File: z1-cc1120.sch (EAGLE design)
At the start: 12 parts, among them X1 PN61729-S

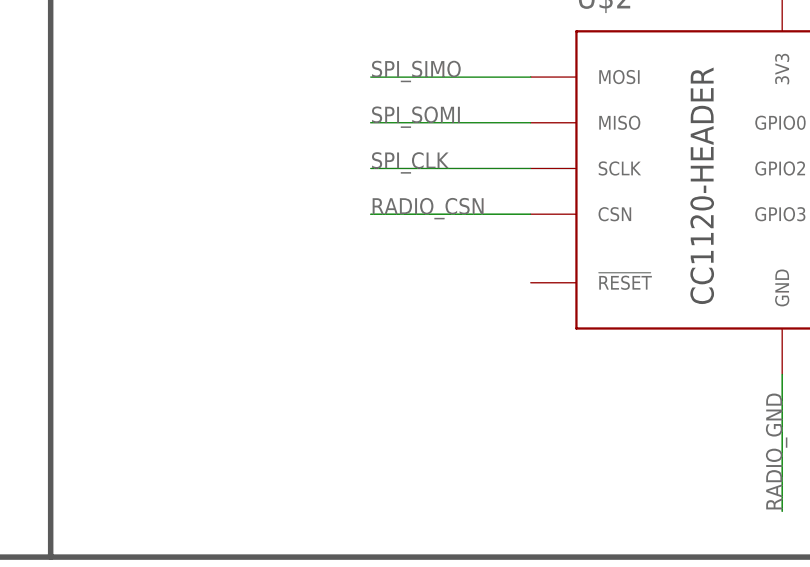
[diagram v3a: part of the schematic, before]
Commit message: !RESET pullup added
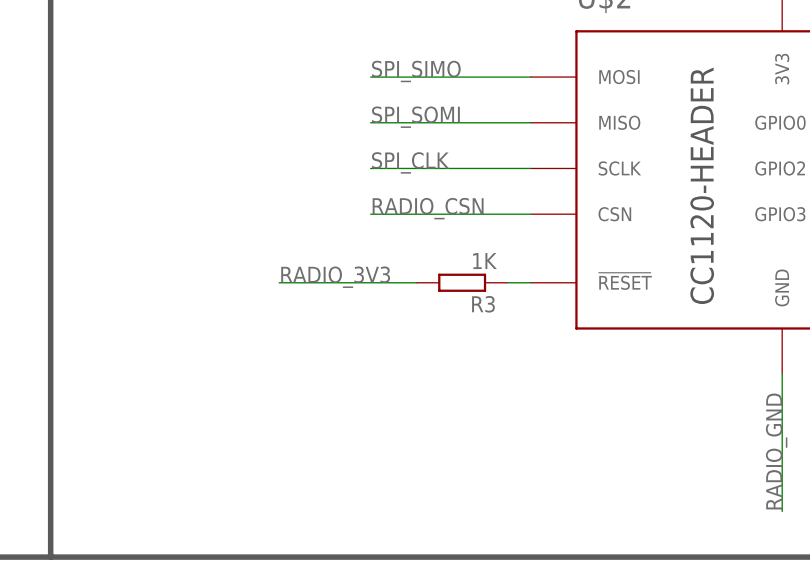
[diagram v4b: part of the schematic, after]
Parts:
- added R3: 1K, resistor:R-EU_R0805
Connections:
- new net N$1: R3.1, U$2.!RESET
- net RADIO_3V3: now also R3.2
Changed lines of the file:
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@@
 <part name="JP1" library="pinhead" deviceset="PINHD-1X6" device=""/>
 <part name="GND3" library="supply1" deviceset="GND" device=""/>
+<part name="R3" library="resistor" deviceset="R-EU_" device="R0805" value="1K"/>
 </parts>
 <sheets>
@@
 <instance part="JP1" gate="A" x="172.72" y="152.4"/>
 <instance part="GND3" gate="1" x="160.02" y="144.78"/>
+<instance part="R3" gate="G$1" x="175.26" y="93.98" rot="R180"/>
 </instances>
 <busses>
@@
 <wire x1="165.1" y1="45.72" x2="182.88" y2="45.72" width="0.1524" layer="91"/>
 </segment>
-</net>
+<segment>
+<pinref part="R3" gate="G$1" pin="2"/>
+<wire x1="170.18" y1="93.98" x2="154.94" y2="93.98" width="0.1524" layer="91"/>
+<label x="154.94" y="93.98" size="1.778" layer="95"/>
+</segment>
+</net>
+<net name="N$1" class="0">
+<segment>
+<pinref part="U$2" gate="G$1" pin="!RESET"/>
+<pinref part="R3" gate="G$1" pin="1"/>
+<wire x1="182.88" y1="93.98" x2="180.34" y2="93.98" width="0.1524" layer="91"/>
+</segment>
+</net>

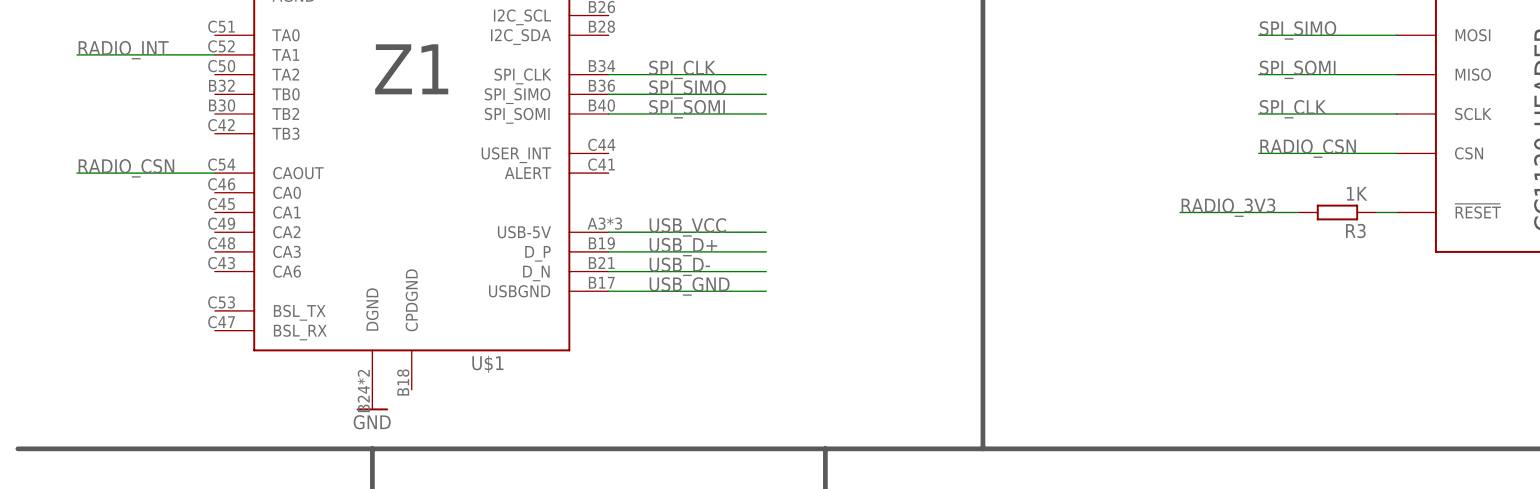
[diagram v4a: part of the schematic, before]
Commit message: Added reset line from msp to cc1120
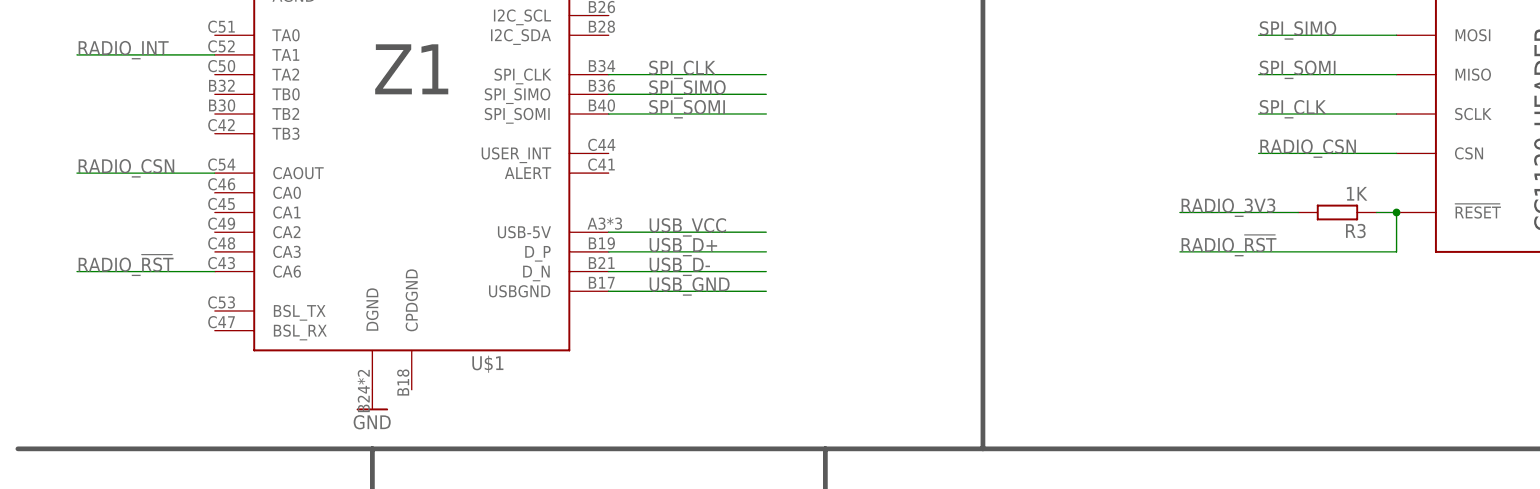
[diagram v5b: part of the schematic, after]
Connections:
- removed net N$1: R3.1, U$2.!RESET
- new net RADIO_!RST: R3.1, U$1.CA6, U$2.!RESET
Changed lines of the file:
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@@
 </segment>
 </net>
-<net name="N$1" class="0">
+<net name="RADIO_!RST" class="0">
 <segment>
 <pinref part="U$2" gate="G$1" pin="!RESET"/>
 <pinref part="R3" gate="G$1" pin="1"/>
 <wire x1="182.88" y1="93.98" x2="180.34" y2="93.98" width="0.1524" layer="91"/>
+<wire x1="182.88" y1="93.98" x2="182.88" y2="88.9" width="0.1524" layer="91"/>
+<wire x1="182.88" y1="88.9" x2="154.94" y2="88.9" width="0.1524" layer="91"/>
+<junction x="182.88" y="93.98"/>
+<label x="154.94" y="88.9" size="1.778" layer="95"/>
+</segment>
+<segment>
+<pinref part="U$1" gate="G$1" pin="CA6"/>
+<wire x1="30.48" y1="86.36" x2="12.7" y2="86.36" width="0.1524" layer="91"/>
+<label x="12.7" y="86.36" size="1.778" layer="95"/>
 </segment>
 </net>

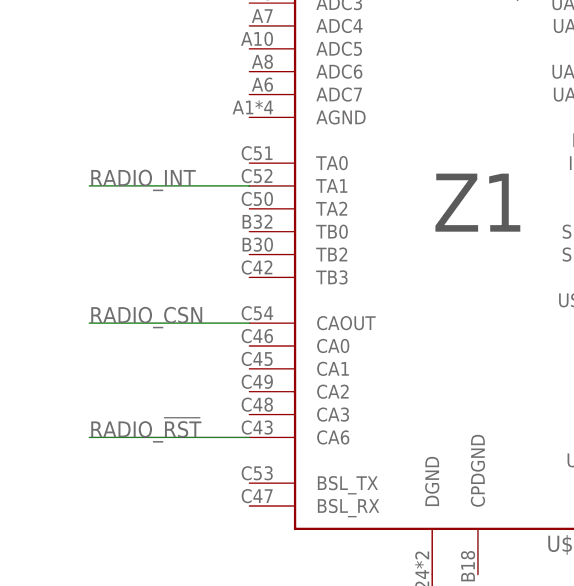
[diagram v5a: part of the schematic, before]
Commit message: pins now changed to match test rig
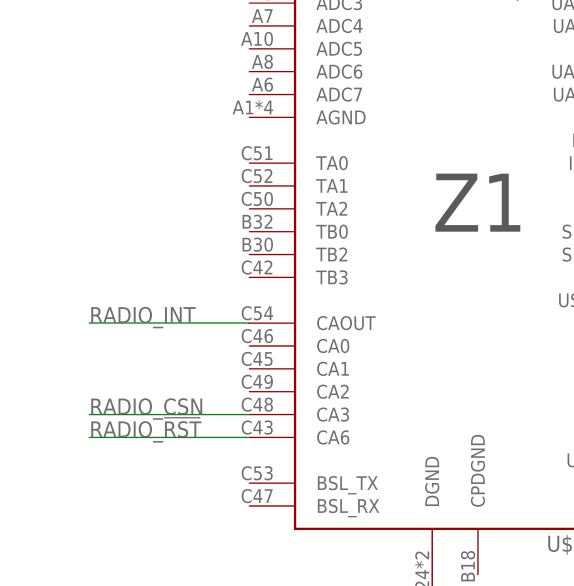
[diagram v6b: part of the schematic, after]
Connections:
- net RADIO_CSN: now also U$1.CA3; no longer U$1.CAOUT
- net RADIO_INT: now also U$1.CAOUT; no longer U$1.TA1
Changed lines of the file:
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@@
-</segment>
-<segment>
-<pinref part="U$1" gate="G$1" pin="CAOUT"/>
-<wire x1="30.48" y1="99.06" x2="12.7" y2="99.06" width="0.1524" layer="91"/>
-<label x="12.7" y="99.06" size="1.778" layer="95"/>
 </segment>
 <segment>
@@
 <wire x1="170.18" y1="152.4" x2="149.86" y2="152.4" width="0.1524" layer="91"/>
 <label x="149.86" y="152.4" size="1.778" layer="95"/>
+</segment>
+<segment>
+<pinref part="U$1" gate="G$1" pin="CA3"/>
+<wire x1="30.48" y1="88.9" x2="12.7" y2="88.9" width="0.1524" layer="91"/>
+<label x="12.7" y="88.9" size="1.778" layer="95"/>
 </segment>
 </net>
@@
 <net name="RADIO_INT" class="0">
 <segment>
-<pinref part="U$1" gate="G$1" pin="TA1"/>
-<wire x1="30.48" y1="114.3" x2="12.7" y2="114.3" width="0.1524" layer="91"/>
-<label x="12.7" y="114.3" size="1.778" layer="95"/>
-</segment>
-<segment>
 <pinref part="U$2" gate="G$1" pin="GPIO0"/>
 <wire x1="220.98" y1="111.76" x2="243.84" y2="111.76" width="0.1524" layer="91"/>
@@
 <label x="149.86" y="149.86" size="1.778" layer="95"/>
 </segment>
+<segment>
+<pinref part="U$1" gate="G$1" pin="CAOUT"/>
+<wire x1="30.48" y1="99.06" x2="12.7" y2="99.06" width="0.1524" layer="91"/>
+<label x="12.7" y="99.06" size="1.778" layer="95"/>
+</segment>
 </net>
